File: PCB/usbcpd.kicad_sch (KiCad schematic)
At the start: 24 parts, among them J4 USB_C_Receptacle_USB2.0, Q2 SSM6J507NU, U1 STUSB4500QTR

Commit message: schematic done and bom ok
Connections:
- net v_{USB}: no longer names the net of C1.1, C3.2, D3.1 (K), D5.2 (A), J4.A4 (VBUS), J4.A9 (VBUS), J4.B4 (VBUS), J4.B9 (VBUS), Q2.4 (S), Q2.8 (S), R4.1, R9.2, U1.24 (VDD)
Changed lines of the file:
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@@
-    (effects (font (size 1.27 1.27)) (justify left bottom))
-  )
-  (label "v_{USB}" (at 59.69 74.93 0) (fields_autoplaced)
     (effects (font (size 1.27 1.27)) (justify left bottom))
   )

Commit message: add 3d models
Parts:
- R2, R3: footprint (none) -> Resistor_SMD:R_0603_1608Metric
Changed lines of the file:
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@@
       (effects (font (size 1.27 1.27)))
     )
-    (property "Footprint" "" (at 151.638 137.16 90)
+    (property "Footprint" "Resistor_SMD:R_0603_1608Metric" (at 151.638 137.16 90)
       (effects (font (size 1.27 1.27)) hide)
     )
@@
       (effects (font (size 1.27 1.27)))
     )
-    (property "Footprint" "" (at 144.018 137.16 90)
+    (property "Footprint" "Resistor_SMD:R_0603_1608Metric" (at 144.018 137.16 90)
       (effects (font (size 1.27 1.27)) hide)
     )

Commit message: routage en cours
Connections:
- net VBUS_USB: now reaches C1.1, C3.2, D3.1 (K), D5.2 (A), J4.A4 (VBUS), J4.A9 (VBUS), J4.B4 (VBUS), J4.B9 (VBUS), Q2.4 (S), Q2.8 (S), R4.1, R9.2, U1.24 (VDD)
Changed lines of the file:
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@@
 (kicad_sch (version 20230121) (generator eeschema)
   (paper "A4")
+  (junction (at 49.53 74.93) (diameter 0) (color 0 0 0 0)
+  )
   (junction (at 143.51 115.57) (diameter 0) (color 0 0 0 0)
   )
@@
     (stroke (width 0) (type default))
   )
+  (wire (pts (xy 49.53 74.93) (xy 58.42 74.93))
+    (stroke (width 0) (type default))
+  )
   (wire (pts (xy 64.77 114.3) (xy 69.85 114.3))
     (stroke (width 0) (type default))
@@
     (stroke (width 0) (type default))
   )
-  (wire (pts (xy 40.64 74.93) (xy 58.42 74.93))
+  (wire (pts (xy 40.64 74.93) (xy 49.53 74.93))
     (stroke (width 0) (type default))
   )
@@
   )
   (wire (pts (xy 143.51 114.3) (xy 143.51 115.57))
+    (stroke (width 0) (type default))
+  )
+  (wire (pts (xy 49.53 73.66) (xy 49.53 74.93))
     (stroke (width 0) (type default))
   )
@@
     (effects (font (size 1.27 1.27)) (justify right bottom))
   )
+  (label "VBUS_USB" (at 49.53 73.66 90) (fields_autoplaced)
+    (effects (font (size 1.27 1.27)) (justify left bottom))
+  )
   (hierarchical_label "I2C{I2C}" (shape bidirectional) (at 157.48 125.73 180) (fields_autoplaced)

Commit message: almost done routing
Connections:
- net CC1: now also D2.2 (K2); no longer D2.1 (K1)
- net CC2: now also D2.1 (K1); no longer D2.2 (K2)
- net USB2.D+: now also D4.1 (K1); no longer D4.2 (K2)
- net USB2.D-: now also D4.2 (K2); no longer D4.1 (K1)
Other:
- moved on the sheet: D4
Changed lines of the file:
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@@
     (effects (font (size 1.27 1.27)) (justify left bottom))
   )
-  (label "CC1" (at 54.61 158.75 90) (fields_autoplaced)
+  (label "CC1" (at 59.69 158.75 90) (fields_autoplaced)
     (effects (font (size 1.27 1.27)) (justify left bottom))
   )
-  (label "CC2" (at 59.69 158.75 90) (fields_autoplaced)
+  (label "CC2" (at 54.61 158.75 90) (fields_autoplaced)
     (effects (font (size 1.27 1.27)) (justify left bottom))
   )
@@
     )
   )
-  (symbol (lib_id "Power_Protection:RCLAMP0502B") (at 72.39 127 90) (unit 1)
-    (in_bom yes) (on_board yes) (dnp no) (fields_autoplaced)
-    (property "Reference" "D4" (at 77.47 126.3015 90)
+  (symbol (lib_id "Power_Protection:RCLAMP0502B") (at 72.39 127 270) (mirror x) (unit 1)
+    (in_bom yes) (on_board yes) (dnp no)
+    (property "Reference" "D4" (at 80.01 125.73 90)
       (effects (font (size 1.27 1.27)) (justify right))
     )
-    (property "Value" "PACDN042Y3R" (at 77.47 128.8415 90)
+    (property "Value" "PACDN042Y3R" (at 91.44 128.27 90)
       (effects (font (size 1.27 1.27)) (justify right))
     )
-    (property "Footprint" "Package_TO_SOT_SMD:SOT-23-3" (at 80.01 127 0)
-      (effects (font (size 1.27 1.27)) hide)
-    )
-    (property "Datasheet" "" (at 69.85 125.73 0)
-      (effects (font (size 1.27 1.27)) hide)
-    )
+    (property "Footprint" "Package_TO_SOT_SMD:SOT-23-3" (at 64.77 127 0)
+      (effects (font (size 1.27 1.27)) hide)
+    )
+    (property "Datasheet" "" (at 74.93 125.73 0)
+      (effects (font (size 1.27 1.27)) hide)
+    )

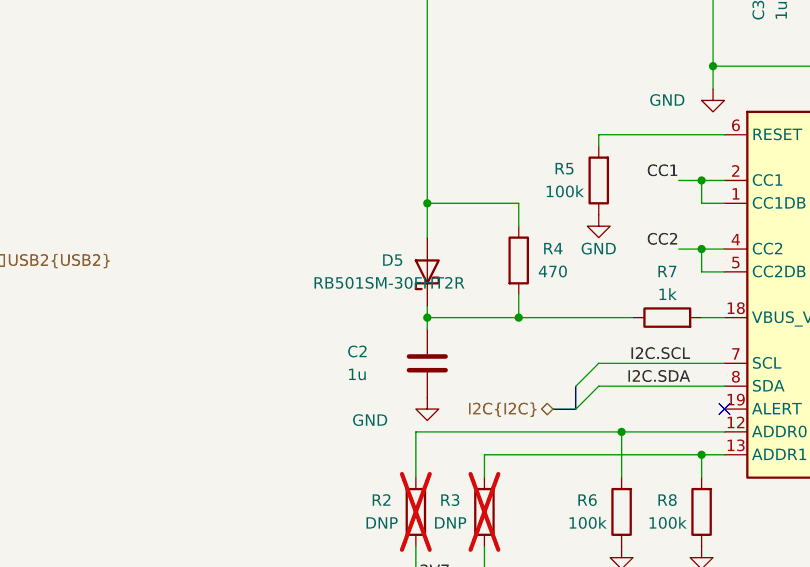
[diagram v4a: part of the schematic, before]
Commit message: switch kicad 8 and change USB connector
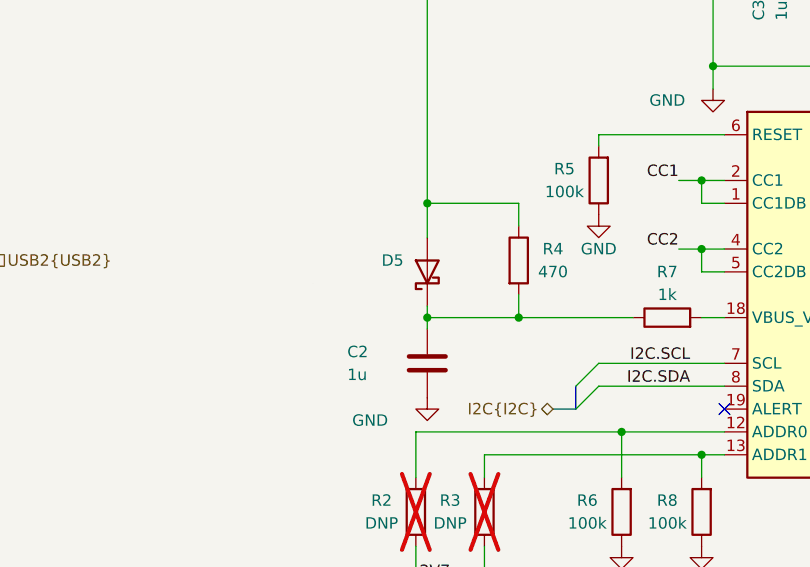
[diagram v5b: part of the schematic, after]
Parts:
- J4: footprint Connector_USB:USB_C_Receptacle_GCT_USB4105-xx-A_16P_TopMnt_Horizontal -> TattooSupplyFootprints:MOLEX_2137160001; MPN GCT -> Molex; Manufacturer USB4105-GF-A -> 213716-0001
